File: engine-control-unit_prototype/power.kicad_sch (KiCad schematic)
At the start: 84 parts, among them IC1 TPS259573DSGR, J8 2S_18650, J9 EXT_BATT, U2 INA3221, U3 AZ1117-3.3, U4 TPS55285, U5 LT3042xMSE, U6 TPS55285, U7 LT3042xMSE

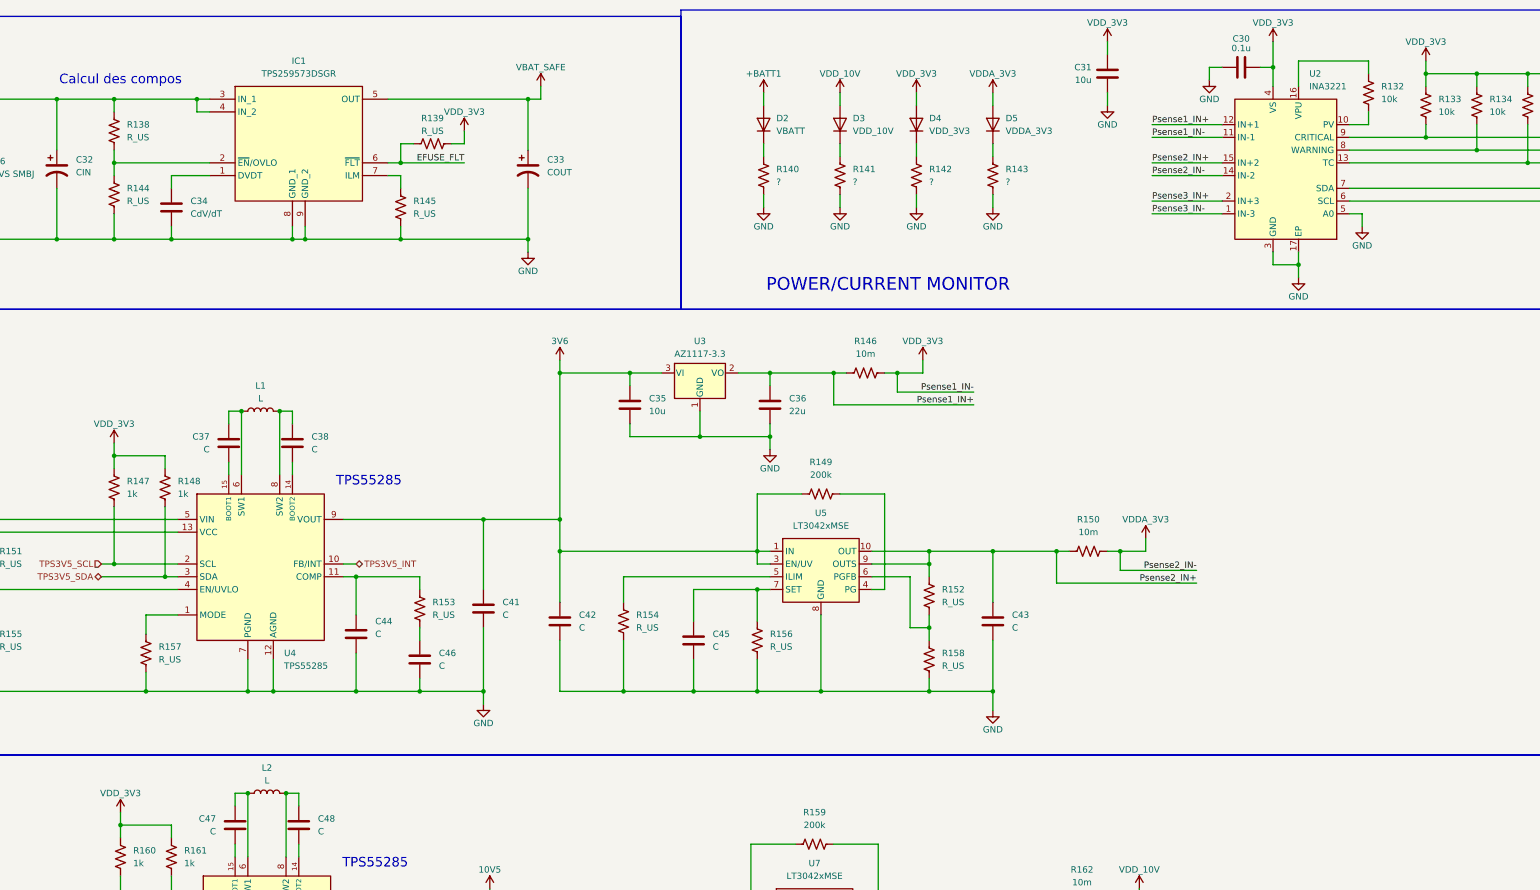
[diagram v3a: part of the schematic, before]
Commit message: VDD_3V3 is now VDD_3V6 (Removed LDO) LEDs now have the right symbol (oops x2)
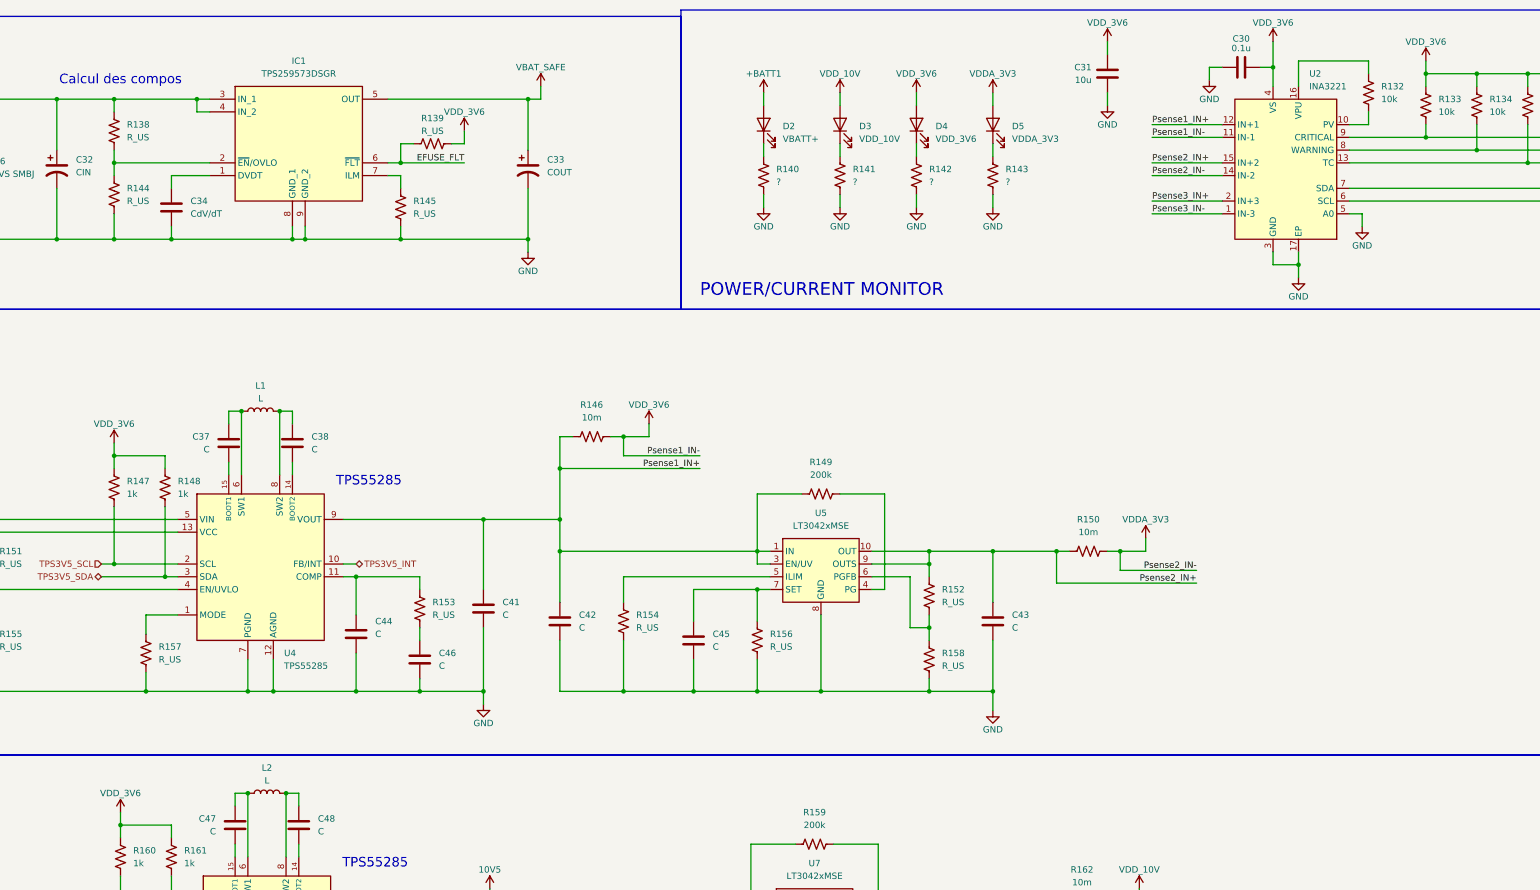
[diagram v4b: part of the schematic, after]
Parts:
- removed C35: 10u, Capacitor_SMD:C_0603_1608Metric, symbol Device:C
- removed C36: 22u, Capacitor_SMD:C_0603_1608Metric, symbol Device:C
- removed D2: VBATT, symbol Device:D
- removed D3: VDD_10V, symbol Device:D
- removed D4: VDD_3V3, symbol Device:D
- removed D5: VDDA_3V3, symbol Device:D
- removed U3: AZ1117-3.3, symbol Regulator_Linear:AZ1117-3.3
- added D2: VBATT+, symbol Device:LED
- added D3: VDD_10V, symbol Device:LED
- added D4: VDD_3V6, symbol Device:LED
- added D5: VDDA_3V3, symbol Device:LED
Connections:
- net 3V6 is gone; now on net Psense1_IN+: C41.1, C42.1, R149.1, U4.9 (VOUT), U5.1 (IN), U5.2 (IN), U5.3 (EN/UV)
- net +BATT1: now also D2.2 (A)
- net VDDA_3V3: now also D5.2 (A)
- net VDD_10V: now also D3.2 (A)
- net at R142.1: now also D4.1 (K)
- net at R143.1: now also D5.1 (K)
- net at R141.1: now also D3.1 (K)
- net at R140.1: now also D2.1 (K)
- net VDD_3V3 renamed VDD_3V6
- net VDD_3V6: now also D4.2 (A)
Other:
- moved on the sheet: R146

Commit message: Started layout Added some footprints
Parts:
- removed R157, R163, R166, R169, R170: R_US, Resistor_SMD:R_0603_1608Metric, symbol Device:R_US
- removed R160, R161: 1k, Resistor_SMD:R_0402_1005Metric, symbol Device:R_US
- added C100, C102, C92, C93, C99: C, Capacitor_SMD:C_0402_1005Metric, symbol Device:C
- added C101, C106, C35: C, Capacitor_SMD:C_1206_3216Metric, symbol Device:C
- added C103, C94: 100p, Capacitor_SMD:C_0402_1005Metric, symbol Device:C
- added C104, C95: ?, Capacitor_SMD:C_0402_1005Metric, symbol Device:C
- added C105, C36, C96, C98: C, Capacitor_SMD:C_0603_1608Metric, symbol Device:C
- added L3: L, Inductor_SMD:L_Coilcraft_XAL7070-XXX, symbol Device:L
- added R121, R123, R127, R129: 2k20, Resistor_SMD:R_0402_1005Metric, symbol Device:R_US
- added R122, R128: 0, Resistor_SMD:R_0402_1005Metric, symbol Device:R_US
- added R124, R130: 27k4, Resistor_SMD:R_0402_1005Metric, symbol Device:R_US
- added R125, R126: R_US, Resistor_SMD:R_0603_1608Metric, symbol Device:R_US
- added R131, R6, R7: R_US, Resistor_SMD:R_0402_1005Metric, symbol Device:R_US
- added U3: TPS55285, Library:WQFN-HR - 15, symbol SiriusLib:TPS55285
- C30: value 0.1u -> 0u1
- C34: footprint Capacitor_SMD:C_0603_1608Metric -> (none)
- C37, C42, C43, C45, C51, C52: footprint Capacitor_SMD:C_0603_1608Metric -> Capacitor_SMD:C_1206_3216Metric
- C40, C41, C44, C56: footprint Capacitor_SMD:C_0603_1608Metric -> Capacitor_SMD:C_0402_1005Metric
- C46: value C -> 100p; footprint Capacitor_SMD:C_0603_1608Metric -> Capacitor_SMD:C_0402_1005Metric
- C47: value C -> ?; footprint Capacitor_SMD:C_0603_1608Metric -> Capacitor_SMD:C_0402_1005Metric
- C49, C50, C54: value C -> 4u7; footprint Capacitor_SMD:C_0603_1608Metric -> Capacitor_SMD:C_1206_3216Metric
- D2, D3, D5: footprint (none) -> LED_SMD:LED_0603_1608Metric
- D4: value VDD_3V6 -> VDD_3V3; footprint (none) -> LED_SMD:LED_0603_1608Metric
- IC1: footprint SON50P200X200X80-9N -> Package_SON:WSON-8-1EP_2x2mm_P0.5mm_EP0.9x1.6mm
- J8: footprint (none) -> Connector_PinSocket_2.54mm:PinSocket_1x02_P2.54mm_Vertical
- J9: footprint (none) -> Connector_PinSocket_2.54mm:PinSocket_1x01_P2.54mm_Vertical
- JP1: footprint (none) -> Connector_PinSocket_2.54mm:PinSocket_1x03_P2.54mm_Vertical
- L1, L2: footprint (none) -> Inductor_SMD:L_Coilcraft_XAL7070-XXX
- R132, R133, R134, R135, R149, R159: footprint (none) -> Resistor_SMD:R_0402_1005Metric
- R146, R150, R162: footprint (none) -> Resistor_SMD:R_2512_6332Metric
- R147: value 1k -> R_US
- R148: value 1k -> 2k20
- R151: value R_US -> 0; footprint Resistor_SMD:R_0603_1608Metric -> Resistor_SMD:R_0402_1005Metric
- R153: value R_US -> 2k20; footprint Resistor_SMD:R_0603_1608Metric -> Resistor_SMD:R_0402_1005Metric
- R155: value R_US -> 27k4; footprint Resistor_SMD:R_0603_1608Metric -> Resistor_SMD:R_0402_1005Metric
- R164: value R_US -> 453k
- R165: value R_US -> 510
- R167: value R_US -> 33k2
- R168: value R_US -> 49k9
- U4, U6: footprint (none) -> Library:WQFN-HR - 15
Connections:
- net TPS3V5_INT is gone; now on net TPS10V_INT: U4.10 (FB/INT)
- net GND: now also C37.2, C38.2, C47.2, C48.2, R147.2, R151.2, C101.2, C103.2, C104.2, C105.2, C106.2, C35.2, C36.2, C94.2, C95.2, C96.2, C98.2, C99.2, R122.2, R126.2, R128.2, R7.2, U3.12 (AGND), U3.7 (PGND); no longer C41.2, C44.2, R155.2
- net Psense1_IN+: now also C101.1, C96.1, U3.9 (VOUT); no longer C41.1, C42.1, R149.1, U4.9 (VOUT), U5.1 (IN), U5.2 (IN), U5.3 (EN/UV)
- net TPS10V_INT: no longer U6.10 (FB/INT)
- net TPS10V_SCL: now also U4.2 (SCL), R127.2; no longer U6.2 (SCL)
- net TPS10V_SDA: now also U4.3 (SDA), R129.2; no longer U6.3 (SDA)
- net VBAT_SAFE: now also C52.1, C53.1, U6.5 (VIN), C35.1, C98.1, R131.1, R6.1, U3.5 (VIN); no longer C39.1, R151.1, U4.5 (VIN)
- net at U6.4 (EN/UVLO): now also C56.1, R147.1, R131.2
- net at C40.1: now also U4.4 (EN/UVLO), R125.2, R126.1; no longer U4.13 (VCC)
- net at C46.1: now also U4.11 (COMP), R130.1; no longer R153.2
- net L2_L: now reaches L2.1, U6.6 (SW1)
- net L2_L: now also C100.1; no longer C47.1
- net at U6.15 (BOOT1): now also C100.2; no longer C47.2
- net L2_R: now reaches L2.2, U6.8 (SW2)
- net L2_R: now also C102.1; no longer C48.1
- net at U6.14 (BOOT2): now also C102.2; no longer C48.2
- net L1_R: now reaches L1.2, U4.8 (SW2)
- net L1_R: now also C44.1; no longer C38.1
- net at U4.14 (BOOT2): now also C44.2; no longer C38.2
- net at U6.1 (MODE): now also R151.1
- net at U6.11 (COMP): now also R155.1, C103.1; no longer C55.1
- net TPS3V3A_VCC: now reaches U6.13 (VCC)
- net TPS3V3A_VCC: now also C55.1; no longer C52.1
- net L1_L: now reaches L1.1, U4.6 (SW1)
- net L1_L: now also C41.1; no longer C37.1
- net at U4.15 (BOOT1): now also C41.2; no longer C37.2
- net at U4.1 (MODE): now also R128.1
- net 10V5 renamed TPS10V_VOUT
- net TPS10V_VOUT: now also C48.1, C51.1, U4.9 (VOUT); no longer C53.1, U6.9 (VOUT)
- removed net TPS3V5_SCL: R147.2, U4.2 (SCL)
- net TPS3V5_SDA renamed TPS3V3A_SCL
- net TPS3V3A_SCL: now also U6.2 (SCL); no longer U4.3 (SDA)
- net VDD_3V6 renamed VDD_3V3
- net VDD_3V3: now also R153.1, R121.1, R123.1, R127.1, R129.1; no longer R147.1
- new net: C104.1, R155.2
- new net: C47.1, R130.2
- new net: C94.1, R124.1, U3.11 (COMP)
- new net: C95.1, R124.2
- new net: C93.2, U3.14 (BOOT2)
- new net: C92.2, U3.15 (BOOT1)
- new net: C99.1, R6.2, R7.1, U3.4 (EN/UVLO)
- new net: R122.1, U3.1 (MODE)
- new net L3_L: C92.1, L3.1, U3.6 (SW1)
- new net L3_R: C93.1, L3.2, U3.8 (SW2)
- new net TPS10V_VCC: C39.1, U4.13 (VCC)
- new net TPS10V_VIN: C37.1, C38.1, JP1.2 (C), R125.1, U4.5 (VIN)
- new net TPS3V3A_INT: U6.10 (FB/INT)
- new net TPS3V3A_SDA: R153.2, U6.3 (SDA)
- new net TPS3V3A_VOUT: C105.1, C106.1, C42.1, R149.1, U5.1 (IN), U5.2 (IN), U5.3 (EN/UV), U6.9 (VOUT)
- new net TPS3V3_INT: U3.10 (FB/INT)
- new net TPS3V3_SCL: R121.2, U3.2 (SCL)
- new net TPS3V3_SDA: R123.2, U3.3 (SDA)
- new net TPS3V3_VCC: C36.1, U3.13 (VCC)
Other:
- note added: "3V3A REGULATION"
- note added: "AGND PGND RELIÉS ??"
- note added: "CHECK IF BULK IS REDUNDANT"
- note added: "LT3042 EVALBOARD"
- note added: "TPS55285 EVALBOARD"
- moved on the sheet: C30, C31, C32, C33, C34, C42, C43, C45, C49, C50, C54, D2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

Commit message: Added better LIB tree Continued PCB layout Some fixes Added chip for protection
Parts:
- removed IC1: TPS259573DSGR, Package_SON:WSON-8-1EP_2x2mm_P0.5mm_EP0.9x1.6mm, symbol TPS259573DSGR:TPS259573DSGR
- removed J9: EXT_BATT, Connector_PinSocket_2.54mm:PinSocket_1x01_P2.54mm_Vertical, symbol Connector:Conn_01x01_Pin
- removed JP1: BATT, Connector_PinSocket_2.54mm:PinSocket_1x03_P2.54mm_Vertical, symbol Jumper:Jumper_3_Bridged12
- removed U3, U4, U6: TPS55285, Library:WQFN-HR - 15, symbol SiriusLib:TPS55285
- added C107: 0u01, Capacitor_SMD:C_0603_1608Metric, symbol Device:C
- added C108: C, Capacitor_SMD:C_0603_1608Metric, symbol Device:C
- added D12: SMBJ16A-13-F, Diode_SMD:D_SMB, symbol Device:D_Zener
- added R157: ROUT, Resistor_SMD:R_0603_1608Metric, symbol Device:R_US
- added U13: TPS2595xx, Package_SON:WSON-8-1EP_2x2mm_P0.5mm_EP0.9x1.6mm, symbol FSU_LIB:TPS259573DSGR
- added U3, U4, U6: TPS55285, symbol FSU_LIB:TPS55285
- C32, C33: footprint (none) -> Capacitor_SMD:CP_Elec_6.3x5.4
- C34: value CdV/dT -> Cdv/dt; footprint (none) -> Capacitor_SMD:C_0603_1608Metric
- C43, C50: footprint Capacitor_SMD:C_1206_3216Metric -> ECUlib:C_1206_3216Metric_SplitPads
- D6: value TVS SMBJ -> MBR130T1G; footprint (none) -> Diode_SMD:D_SOD-123
- F1: footprint (none) -> Fuse:Fuse_0805_2012Metric
- J8: value 2S_18650 -> VBATT
- R138: value R_US -> RVL1
- R139: value R_US -> RFLT
- R144: value R_US -> RVL2
- R145: value R_US -> RILIM
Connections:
- net TPS10V_VIN is gone; now on net VBAT_SAFE: C37.1, C38.1, R125.1
- net EFUSE_FLT: now also U13.6 (FLT)
- net GND: now also C107.2, C108.2, D12.2 (A), R157.2, U13.8 (GND), U3.12 (AGND), U3.7 (PGND), U4.12 (AGND), U4.7 (PGND), U6.12 (AGND), U6.7 (PGND)
- net L1_L: now also U4.6 (SW1)
- net L1_R: now also U4.8 (SW2)
- net L2_L: now also U6.6 (SW1)
- net L2_R: now also U6.8 (SW2)
- net L3_L: now also U3.6 (SW1)
- net L3_R: now also U3.8 (SW2)
- net Psense1_IN+: now also U3.9 (VOUT)
- net Psense2_IN+: now also C50.1, R162.1, R164.1, U7.10 (OUT), U7.9 (OUTS); no longer C43.1, R150.1, R152.1, U5.10 (OUT), U5.9 (OUTS)
- net Psense3_IN+: now also C43.1, R150.1, R152.1, U5.10 (OUT), U5.9 (OUTS); no longer C50.1, R162.1, R164.1, U7.10 (OUT), U7.9 (OUTS)
- net TPS10V_INT: now also U4.10 (FB/INT)
- net TPS10V_SCL: now also U4.2 (SCL)
- net TPS10V_SDA: now also U4.3 (SDA)
- net TPS10V_VCC: now also U4.13 (VCC)
- net TPS10V_VOUT: now also U4.9 (VOUT)
- net TPS3V3A_INT: now also U6.10 (FB/INT)
- net TPS3V3A_SCL: now also U6.2 (SCL)
- net TPS3V3A_SDA: now also U6.3 (SDA)
- net TPS3V3A_VCC: now also U6.13 (VCC)
- net TPS3V3A_VOUT: now also U6.9 (VOUT)
- net TPS3V3_INT: now also U3.10 (FB/INT)
- net TPS3V3_SCL: now also U3.2 (SCL)
- net TPS3V3_SDA: now also U3.3 (SDA)
- net TPS3V3_VCC: now also U3.13 (VCC)
- net VBAT_SAFE: now also D6.1 (K), C108.1, R157.1, U13.5 (OUT), U3.5 (VIN), U4.5 (VIN), U6.5 (VIN)
- net VDDA_3V3: now also U2.1 (IN-3); no longer U2.14 (IN-2)
- net VDD_10V: now also U2.14 (IN-2); no longer U2.1 (IN-3)
- net at R145.1: now also U13.7 (ILM)
- net at R138.2, R144.1: now also U13.2 (EN/UVLO)
- net at C46.1, R130.1: now also U4.11 (COMP)
- net at C94.1, R124.1: now also U3.11 (COMP)
- net EFUSE_VBATT: now reaches C32.1, F1.2, R138.1
- net EFUSE_VBATT: now also C107.1, D12.1 (K), U13.3 (IN), U13.4 (IN); no longer D6.1 (K)
- net at C93.2: now also U3.14 (BOOT2)
- net LDO3V3A_PG: now reaches R149.2, U5.4 (PG)
- net LDO3V3A_ILIM: now reaches R154.1, U5.5 (ILIM)
- net LDO3V3A_PGFB: now reaches R152.2, R158.1, U5.6 (PGFB)
- net LDO3V3A_CSET: now reaches C45.1, R156.1, U5.7 (SET)
- net LDO10V_CSET: now reaches C54.1, R167.1, U7.7 (SET)
- net at C34.1: now also U13.1 (dVdt)
- net at R128.1: now also U4.1 (MODE)
- net LDO10V_PG: now reaches R159.2, U7.4 (PG)
- net LDO10V_ILIM: now reaches R165.1, U7.5 (ILIM)
- net LDO10V_PGFB: now reaches R164.2, R168.1, U7.6 (PGFB)
- net at C103.1, R155.1: now also U6.11 (COMP)
- net at C40.1, R125.2, R126.1: now also U4.4 (EN/UVLO)
- net at C56.1, R131.2, R147.1: now also U6.4 (EN/UVLO)
- net at R151.1: now also U6.1 (MODE)
- net at C102.2: now also U6.14 (BOOT2)
- net at C100.2: now also U6.15 (BOOT1)
- net at C44.2: now also U4.14 (BOOT2)
- net at C41.2: now also U4.15 (BOOT1)
- net at C92.2: now also U3.15 (BOOT1)
- net at C99.1, R6.2, R7.1: now also U3.4 (EN/UVLO)
- net at R122.1: now also U3.1 (MODE)
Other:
- moved on the sheet: C32, C33, C34, D2, D3, D4, D5, D6, F1, R138, R139, R140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

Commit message: Continued layout
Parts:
- added D13: LED2, LED_SMD:LED_0603_1608Metric, symbol Device:LED
- added D14: LED3, LED_SMD:LED_0603_1608Metric, symbol Device:LED
- added D8: LED1, LED_SMD:LED_0603_1608Metric, symbol Device:LED
- added R171: ?, Resistor_SMD:R_0603_1608Metric, symbol Device:R_US
- R136, R137: value 10k -> ?; footprint Resistor_SMD:R_0402_1005Metric -> Resistor_SMD:R_0603_1608Metric
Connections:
- net GND: now also R136.2, R137.2, R171.2
- net PM_SCL: no longer R137.2
- net PM_SDA: no longer R136.2
- net VDD_3V3: no longer R136.1, R137.1
- new net: D13.1 (K), R137.1
- new net: D14.1 (K), R171.1
- new net: D8.1 (K), R136.1
- new net LED1: D8.2 (A)
- new net LED2: D13.2 (A)
- new net LED3: D14.2 (A)

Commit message: ajout de page root
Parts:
- renumbered C35 to C1, C32 to C10, C107 to C11, C99 to C12, C40 to C13, C56 to C14, C34 to C15, C92 to C16, C41 to C17, C100 to C18, C93 to C19, C37 to C2, C44 to C20, C102 to C21, C94 to C22, C46 to C23, C103 to C24, C95 to C25, C47 to C26, C104 to C27, C108 to C28, C96 to C29, C52 to C3, C48 to C30, C105 to C31, C33 to C32, C101 to C33, C51 to C34, C106 to C35, C30 to C36, C31 to C37, C49 to C38, C42 to C39, C98 to C4, C54 to C40, C45 to C41, C50 to C42, C38 to C5, C53 to C6, C36 to C7, C39 to C8, C55 to C9, D12 to D1, D6 to D2, D2 to D3, D8 to D4, D13 to D5, D3 to D6, D14 to D7, D4 to D8, D5 to D9, J8 to J1, L3 to L1, L1 to L2, L2 to L3, R6 to R1, R127 to R10, R148 to R11, R122 to R12, R123 to R13, R128 to R14, R151 to R15, R129 to R16, R153 to R17, R145 to R18, R139 to R19, R7 to R2, R124 to R20, R130 to R21, R155 to R22, R146 to R23, R157 to R24, R135 to R25, R134 to R26, R133 to R27, R140 to R28, R136 to R29, R125 to R3, R132 to R30, R137 to R31, R141 to R32, R171 to R33, R142 to R34, R143 to R35, R165 to R36, R154 to R37, R167 to R38, R156 to R39, R126 to R4, R159 to R40, R149 to R41, R164 to R42, R168 to R43, R152 to R44, R158 to R45, R162 to R46, R150 to R47, R131 to R5, R147 to R6, R138 to R7, R144 to R8, R121 to R9, U13 to U1, U3 to U2, U4 to U3, U6 to U4, U2 to U5, U7 to U6, U5 to U7
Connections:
- net TPS10V_VOUT: no longer C38.1, R40.1, U6.1 (IN), U6.2 (IN), U6.3 (EN/UV)
- net TPS3V3A_VOUT: no longer C39.1, R41.1, U7.1 (IN), U7.2 (IN), U7.3 (EN/UV)
- new net: C39.1, R41.1, U7.1 (IN), U7.2 (IN), U7.3 (EN/UV)
- new net: C38.1, R40.1, U6.1 (IN), U6.2 (IN), U6.3 (EN/UV)
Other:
- note added: "resistor a la sortie du tps55285"
- moved on the sheet: C38, C39, C40, C41, C42, C43, R36, R37, R38, R39, R40, R41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
